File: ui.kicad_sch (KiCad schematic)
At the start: 33 parts, among them J19 Conn_01x03_Socket, J2 Conn_01x06_Socket, J20 Conn_01x02_Socket, J21 Conn_01x02_Socket, J22 Conn_01x02_Socket, J23 Conn_01x02_Socket, J4 Conn_01x06_Socket, J6 Conn_01x02_Socket, J7 Conn_01x02_Socket, U3 SN74HC14N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

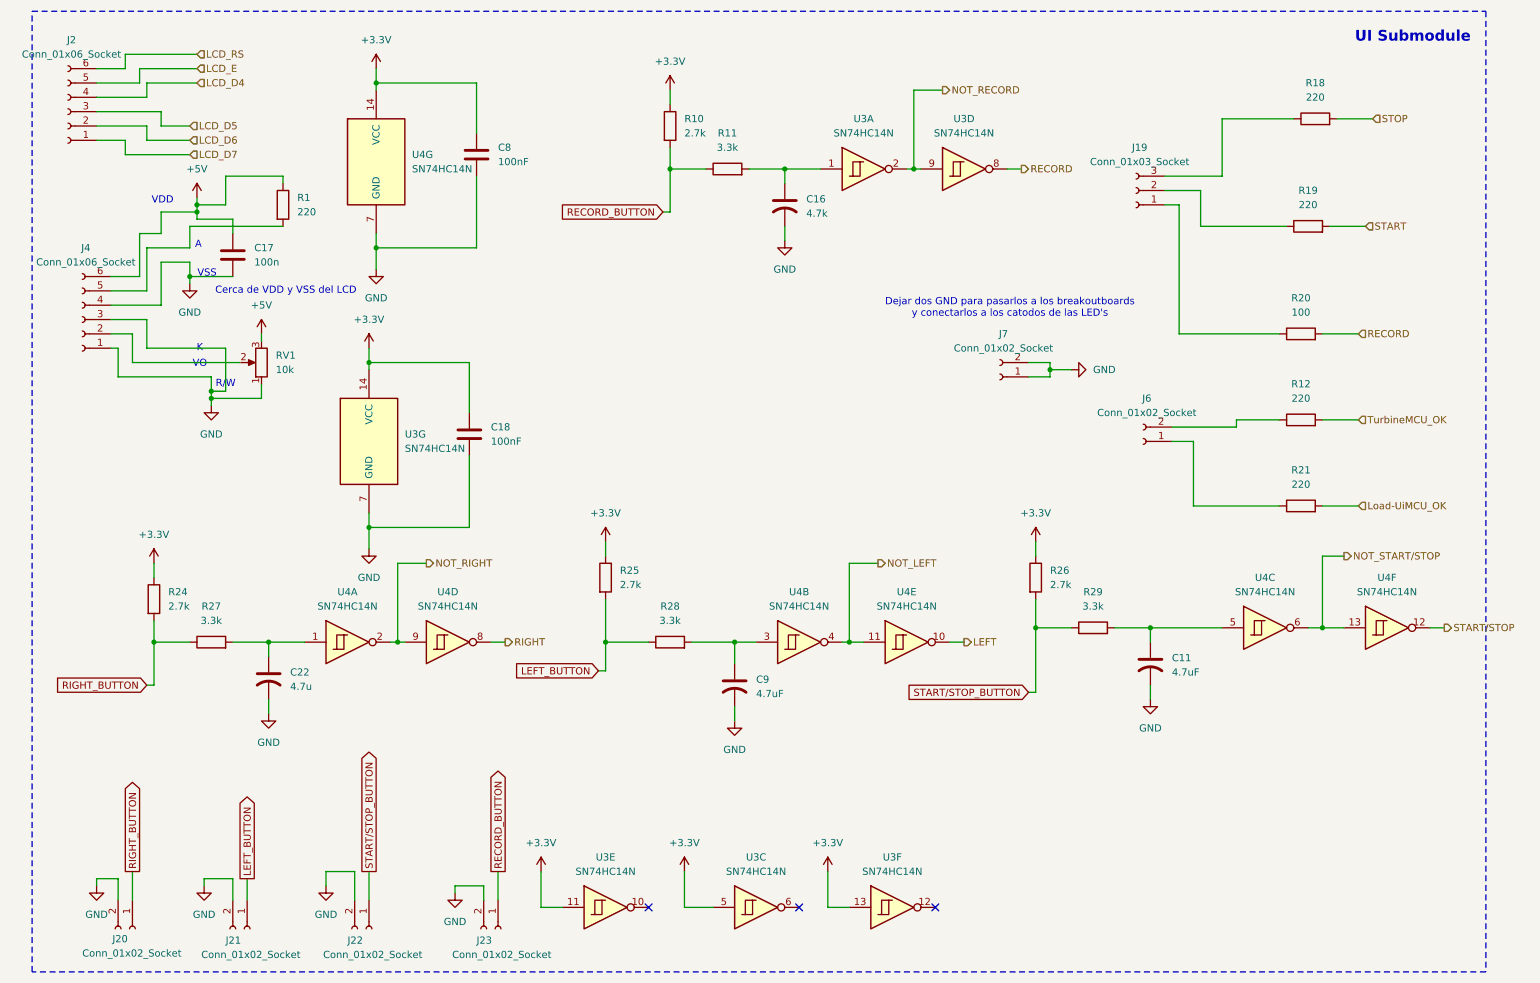
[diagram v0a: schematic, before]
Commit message: Finished pcb for manufacturing, changed some footprints based on what the manufacturer had. Also I fixed the potentiometer footprint.
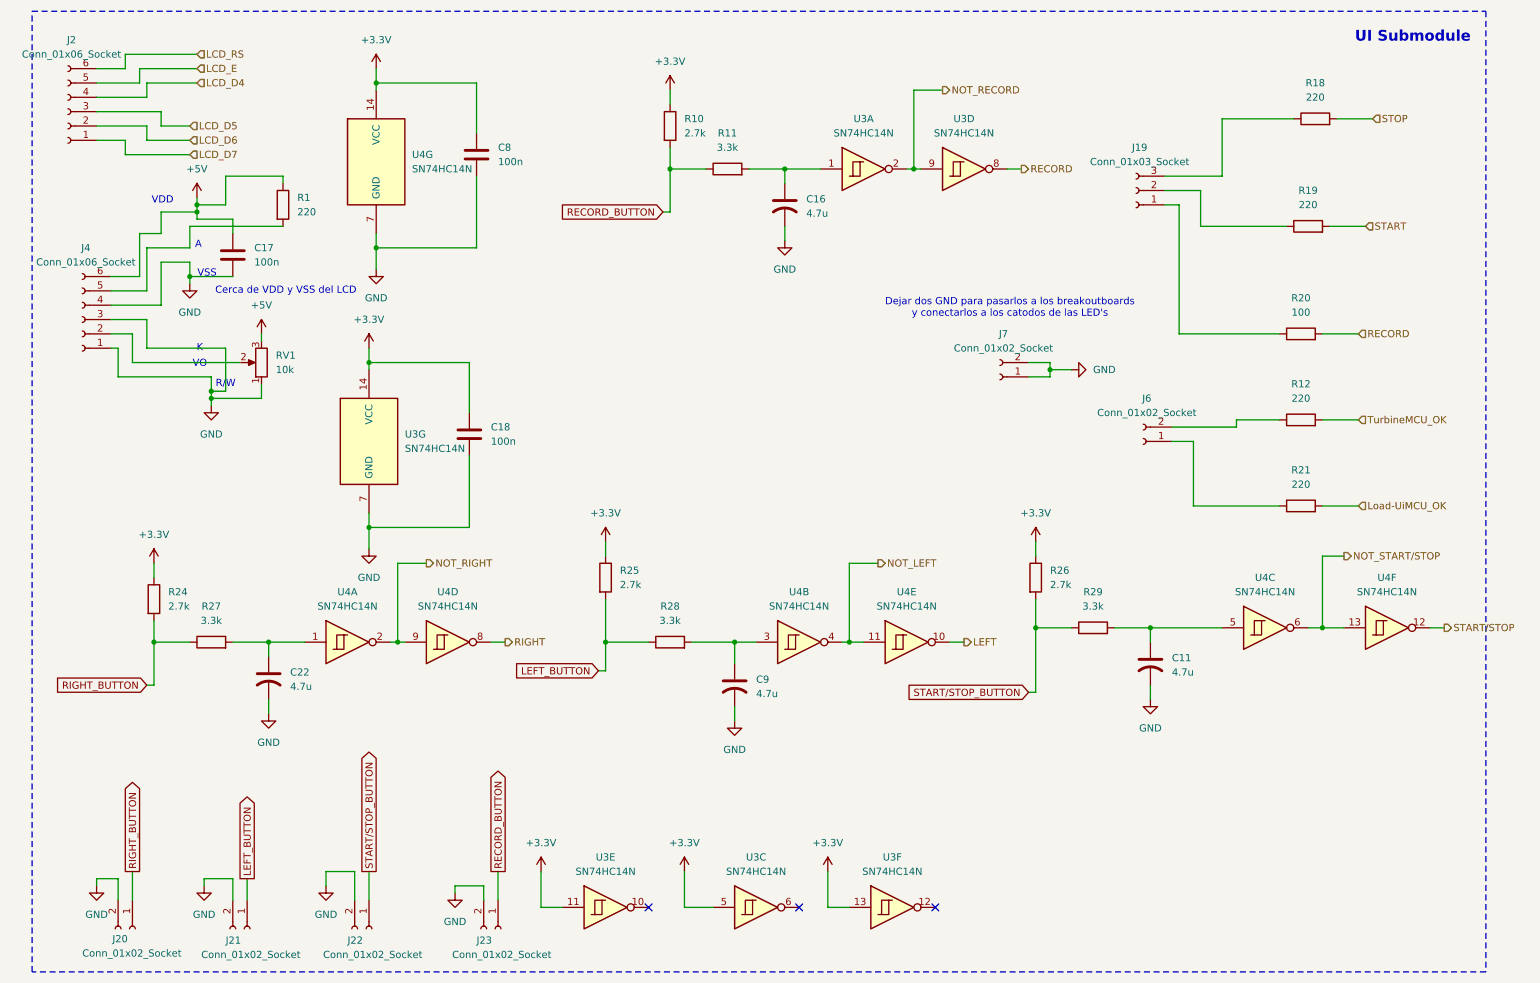
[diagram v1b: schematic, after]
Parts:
- C11, C9: value 4.7uF -> 4.7u
- C16: value 4.7k -> 4.7u; footprint Resistor_SMD:R_1206_3216Metric_Pad1.30x1.75mm_HandSolder -> Capacitor_SMD:C_1206_3216Metric_Pad1.33x1.80mm_HandSolder
- C18, C8: value 100nF -> 100n
- R10, R11, R24, R25, R26, R27, R28, R29: footprint Resistor_SMD:R_1206_3216Metric_Pad1.30x1.75mm_HandSolder -> Resistor_SMD:R_0805_2012Metric_Pad1.20x1.40mm_HandSolder
- RV1: footprint Resistor_SMD:R_1206_3216Metric_Pad1.30x1.75mm_HandSolder -> Potentiometer_THT:Potentiometer_Bourns_3296W_Vertical
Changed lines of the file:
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@@
 			)
 		)
-		(property "Footprint" "Resistor_SMD:R_1206_3216Metric_Pad1.30x1.75mm_HandSolder"
+		(property "Footprint" "Resistor_SMD:R_0805_2012Metric_Pad1.20x1.40mm_HandSolder"
 			(at 135.89 50.038 90)
 			(effects
@@
 			)
 		)
-		(property "Footprint" "Resistor_SMD:R_1206_3216Metric_Pad1.30x1.75mm_HandSolder"
+		(property "Footprint" "Resistor_SMD:R_0805_2012Metric_Pad1.20x1.40mm_HandSolder"
 			(at 125.73 133.858 90)
 			(effects
@@
 			)
 		)
-		(property "Value" "100nF"
+		(property "Value" "100n"
 			(at 93.98 96.5199 0)
 			(effects
@@
 			)
 		)
-		(property "Value" "4.7uF"
+		(property "Value" "4.7u"
 			(at 140.97 141.2239 0)
 			(effects
@@
 			)
 		)
-		(property "Value" "4.7uF"
+		(property "Value" "4.7u"
 			(at 214.63 137.4139 0)
 			(effects
@@
 			)
 		)
-		(property "Footprint" "Resistor_SMD:R_1206_3216Metric_Pad1.30x1.75mm_HandSolder"
+		(property "Footprint" "Resistor_SMD:R_0805_2012Metric_Pad1.20x1.40mm_HandSolder"
 			(at 188.722 120.65 90)
 			(effects
@@
 			)
 		)
-		(property "Footprint" "Resistor_SMD:R_1206_3216Metric_Pad1.30x1.75mm_HandSolder"
+		(property "Footprint" "Resistor_SMD:R_0805_2012Metric_Pad1.20x1.40mm_HandSolder"
 			(at 44.45 133.858 90)
 			(effects
@@
 			)
 		)
-		(property "Footprint" "Resistor_SMD:R_1206_3216Metric_Pad1.30x1.75mm_HandSolder"
+		(property "Footprint" "Resistor_SMD:R_0805_2012Metric_Pad1.20x1.40mm_HandSolder"
 			(at 112.522 120.65 90)
 			(effects
@@
 			)
 		)
-		(property "Value" "4.7k"
+		(property "Value" "4.7u"
 			(at 149.86 56.1339 0)
 			(effects
@@
 			)
 		)
-		(property "Footprint" "Resistor_SMD:R_1206_3216Metric_Pad1.30x1.75mm_HandSolder"
+		(property "Footprint" "Capacitor_SMD:C_1206_3216Metric_Pad1.33x1.80mm_HandSolder"
 			(at 146.05 54.61 0)
 			(effects
@@
 			)
 		)
-		(property "Value" "100nF"
+		(property "Value" "100n"
 			(at 95.25 46.9899 0)
 			(effects
@@
 			)
 		)
-		(property "Footprint" "Resistor_SMD:R_1206_3216Metric_Pad1.30x1.75mm_HandSolder"
+		(property "Footprint" "Resistor_SMD:R_0805_2012Metric_Pad1.20x1.40mm_HandSolder"
 			(at 200.66 131.318 90)
 			(effects
@@
 			)
 		)
-		(property "Footprint" "Resistor_SMD:R_1206_3216Metric_Pad1.30x1.75mm_HandSolder"
+		(property "Footprint" "Resistor_SMD:R_0805_2012Metric_Pad1.20x1.40mm_HandSolder"
 			(at 32.512 124.46 90)
 			(effects
@@
 			)
 		)
-		(property "Footprint" "Resistor_SMD:R_1206_3216Metric_Pad1.30x1.75mm_HandSolder"
+		(property "Footprint" "Potentiometer_THT:Potentiometer_Bourns_3296W_Vertical"
 			(at 53.34 82.55 0)
 			(effects
@@
 			)
 		)
-		(property "Footprint" "Resistor_SMD:R_1206_3216Metric_Pad1.30x1.75mm_HandSolder"
+		(property "Footprint" "Resistor_SMD:R_0805_2012Metric_Pad1.20x1.40mm_HandSolder"
 			(at 123.952 40.64 90)
 			(effects

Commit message: Removed unnecessary hex inverter, fixed record button connection, change relay resistors to smd
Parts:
- removed C8: 100n, Capacitor_SMD:C_0805_2012Metric_Pad1.18x1.45mm_HandSolder, symbol Device:C
- removed U4: SN74HC14N, Package_DIP:CERDIP-14_W7.62mm_SideBrazed, symbol 74xx:74LS14
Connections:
- net +3.3V: no longer U3.11, U3.5
- net LEFT: now also U3.6
- net RECORD: now also U3.2; no longer R20.2, U3.8
- net RIGHT: now also U3.10
- net START/STOP: now also U3.8
- net RECORD_INPUT: now reaches C16.1, R11.2, U3.1
- net LEFT_INPUT: now reaches C9.1, R28.2
- net LEFT_INPUT: now also U3.5
- net RIGHT_INPUT: now reaches C22.1, R27.2
- net RIGHT_INPUT: now also U3.11
- net ST_INPUT: now reaches C11.1, R29.2
- net ST_INPUT: now also U3.9
- removed net NOT_RECORD: U3.2, U3.9
- new net RECORD_L: R20.2
- no-connect marks 3 -> 1
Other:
- moved on the sheet: U3C, U3D, U3E

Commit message: schematic comments
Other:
- note added: "LCD"
- note added: "LED's"
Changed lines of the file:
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@@
+		)
+	)
+	(text "LCD"
+		(exclude_from_sim no)
+		(at 71.12 58.42 0)
+		(effects
+			(font
+				(size 1.27 1.27)
+			)
 		)
 	)
@@
 		(exclude_from_sim no)
 		(at 185.928 72.898 0)
+		(effects
+			(font
+				(size 1.27 1.27)
+			)
+		)
+	)
+	(text "LED's"
+		(exclude_from_sim no)
+		(at 201.676 95.504 0)
 		(effects
 			(font
@@
 		(effects
 			(font
+				(size 1.27 1.27)
+			)
+		)
+	)
+	(text "LED's"
+		(exclude_from_sim no)
+		(at 198.882 52.07 0)
+		(effects
+			(font
